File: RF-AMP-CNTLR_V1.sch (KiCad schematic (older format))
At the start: 57 parts, among them J1 VAC, J10 FWD3, J11 REF3, J12 FWD4, J13 REF4, J14 ALC, J15 AMP1, J16 AMP2, J17 FAN, J18 PTT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

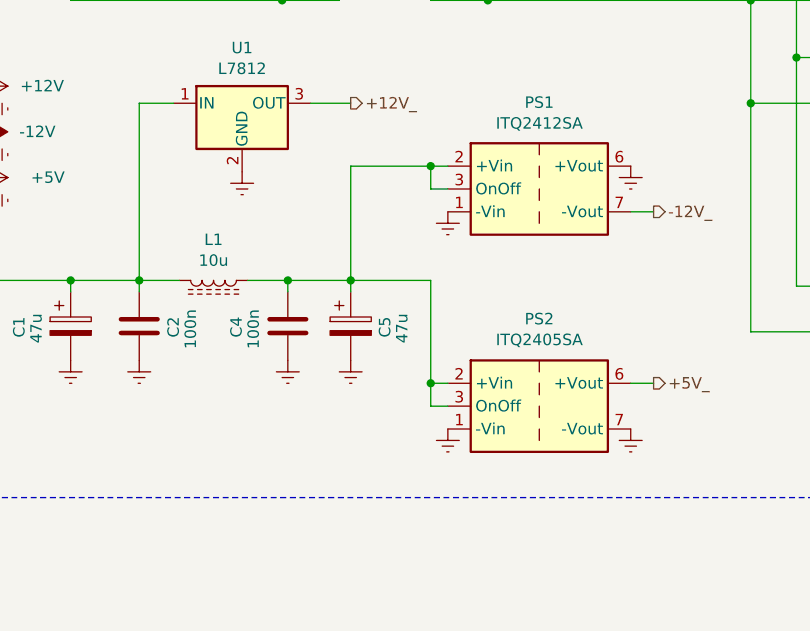
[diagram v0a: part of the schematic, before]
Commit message: bug fix ITQ ON/OFF
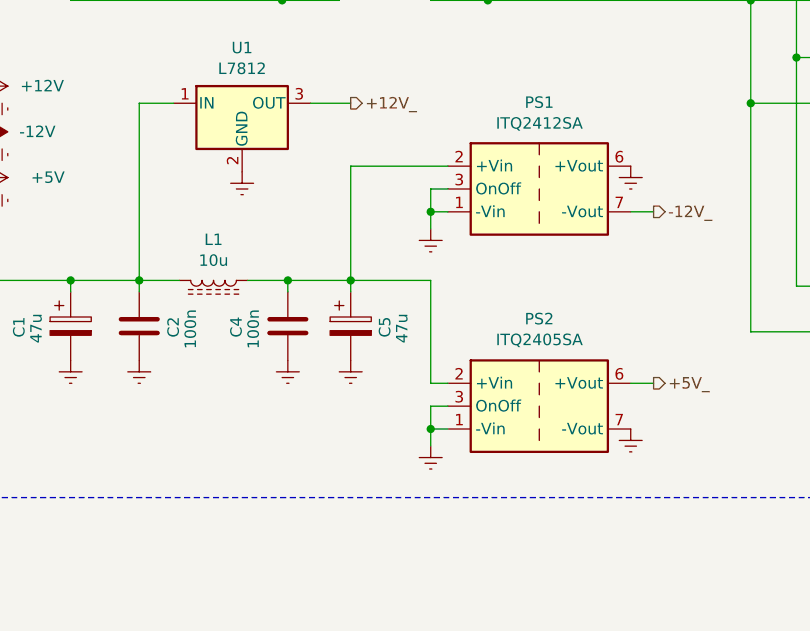
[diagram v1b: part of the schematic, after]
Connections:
- net CONTROLLER/PTT_ is gone; now on net CONTROLLER/PTT_: J19.14 (Pin_14)
- net CONTROLLER/PTT_: no longer J18.1 (In)
- net Earth: now also PS1.3 (OnOff), PS2.3 (OnOff)
- net at C4.1, C5.1, L1.1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: no longer PS1.3 (OnOff), PS2.3 (OnOff)
- new net CONTROLLER/PTT_: J18.1 (In)
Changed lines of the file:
@@
 Wire Wire Line
 	3200 2800 3200 2300
-Wire Wire Line
-	3200 2300 3550 2300
 Connection ~ 3200 2800
 Wire Wire Line
@@
 L power:Earth #PWR025
 U 1 1 5D5B9FA3
-P 3625 2500
+P 3550 2575
 AR Path="/5D5B9FA3" Ref="#PWR025"  Part="1"
 AR Path="/5C000D65/5D5B9FA3" Ref="#PWR?"  Part="1"
 AR Path="/5CBB0B33/5D5B9FA3" Ref="#PWR?"  Part="1"
-F 0 "#PWR025" H 3625 2250 50  0001 C CNN
-F 1 "Earth" H 3625 2350 50  0001 C CNN
-F 2 "" H 3625 2500 50  0001 C CNN
-F 3 "" H 3625 2500 50  0001 C CNN
-	1    3625 2500
+F 0 "#PWR025" H 3550 2325 50  0001 C CNN
+F 1 "Earth" H 3550 2425 50  0001 C CNN
+F 2 "" H 3550 2575 50  0001 C CNN
+F 3 "" H 3550 2575 50  0001 C CNN
+	1    3550 2575
 	1    0    0    -1
 $EndComp
@@
 L power:Earth #PWR026
 U 1 1 5D5BA03B
-P 3625 3450
+P 3550 3525
 AR Path="/5D5BA03B" Ref="#PWR026"  Part="1"
 AR Path="/5C000D65/5D5BA03B" Ref="#PWR?"  Part="1"
 AR Path="/5CBB0B33/5D5BA03B" Ref="#PWR?"  Part="1"
-F 0 "#PWR026" H 3625 3200 50  0001 C CNN
-F 1 "Earth" H 3625 3300 50  0001 C CNN
-F 2 "" H 3625 3450 50  0001 C CNN
-F 3 "" H 3625 3450 50  0001 C CNN
-	1    3625 3450
+F 0 "#PWR026" H 3550 3275 50  0001 C CNN
+F 1 "Earth" H 3550 3375 50  0001 C CNN
+F 2 "" H 3550 3525 50  0001 C CNN
+F 3 "" H 3550 3525 50  0001 C CNN
+	1    3550 3525
 	1    0    0    -1
 $EndComp
@@
 	3625 2400 3550 2400
 Wire Wire Line
-	3550 2400 3550 2300
-Connection ~ 3550 2300
-Wire Wire Line
-	3550 2300 3625 2300
-Wire Wire Line
 	3625 3350 3550 3350
-Wire Wire Line
-	3550 3350 3550 3250
-Connection ~ 3550 3250
 Text HLabel 3200 2025 2    50   Output ~ 0
 +12V_
@@
 Wire Wire Line
 	10275 6150 11025 6150
+Wire Wire Line
+	3200 2300 3625 2300
+Wire Wire Line
+	3550 2400 3550 2500
+Wire Wire Line
+	3625 2500 3550 2500
+Connection ~ 3550 2500
+Wire Wire Line
+	3550 2500 3550 2575
+Wire Wire Line
+	3550 3350 3550 3450
+Wire Wire Line
+	3625 3450 3550 3450
+Connection ~ 3550 3450
+Wire Wire Line
+	3550 3450 3550 3525
 $EndSCHEMATC

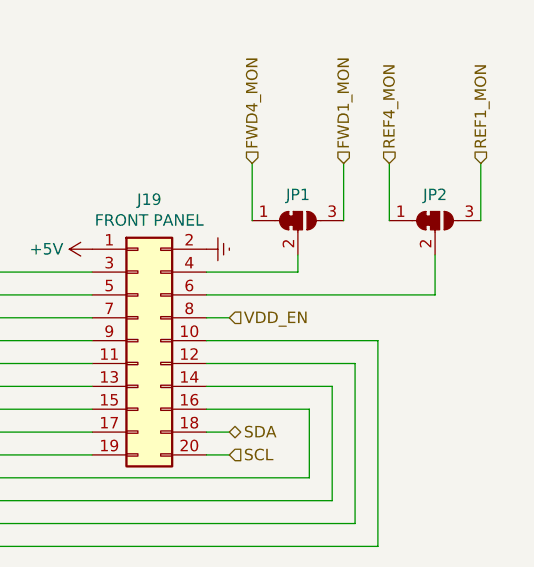
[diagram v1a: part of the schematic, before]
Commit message: ALC latch-up fix
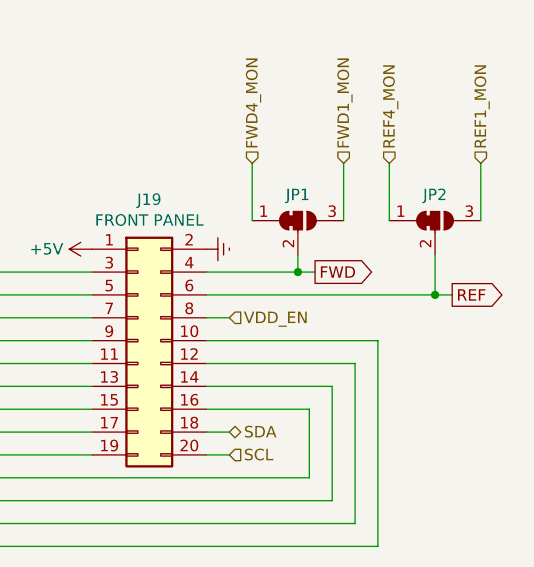
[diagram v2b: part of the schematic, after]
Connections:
- net CONTROLLER/PTT_ is gone; now on net CONTROLLER/PTT_: J19.14 (Pin_14)
- net CONTROLLER/PTT_: no longer J18.1 (In)
- net FWD: now reaches J19.4 (Pin_4), JP1.2 (C)
- net REF: now reaches J19.6 (Pin_6), JP2.2 (C)
- new net CONTROLLER/PTT_: J18.1 (In)
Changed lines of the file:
@@
 Sheet 1 3
 Title "RF Amplifier Controller"
-Date "2020-07-24"
+Date "2020-10-25"
 Rev "1"
 Comp "HB9GKW"
@@
 Wire Wire Line
 	3550 3450 3550 3525
+Text GLabel 10750 5850 2    50   Output ~ 0
+FWD
+Wire Wire Line
+	10675 5850 10750 5850
+Connection ~ 10675 5850
+Text GLabel 11350 5950 2    50   Output ~ 0
+REF
+Wire Wire Line
+	11350 5950 11275 5950
+Connection ~ 11275 5950
 $EndSCHEMATC
